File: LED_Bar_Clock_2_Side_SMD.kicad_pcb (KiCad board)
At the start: 2 copper layers, 100 x 100 mm, 51 parts, among them J1 U262-16XN-4BVC11, J2 AVR-ISP-6, SW1 SKHMQKE010, SW2 SW_5_Way, U1 ATtiny84A-SSUR, U2 DS1307Z+, Y1 32.768 kHz

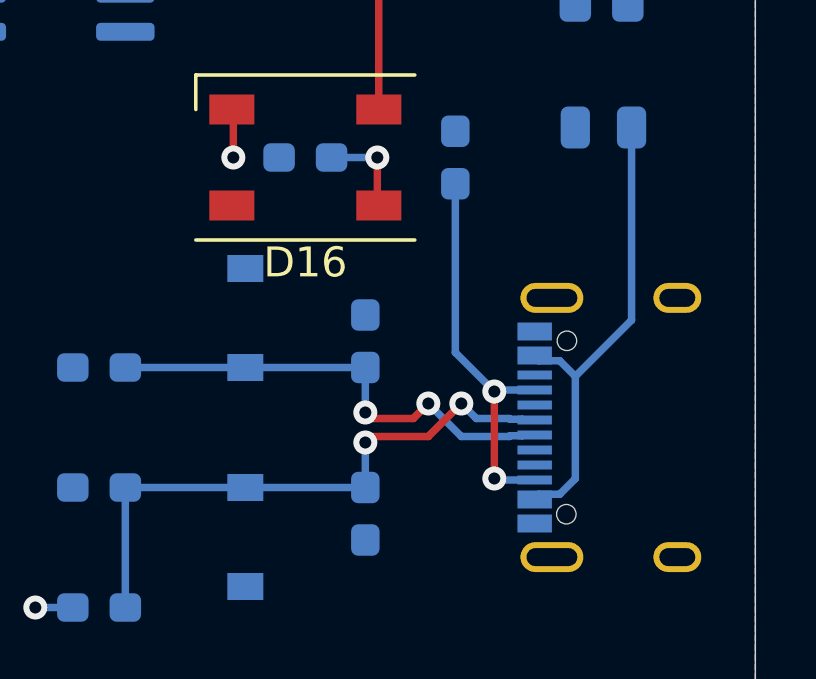
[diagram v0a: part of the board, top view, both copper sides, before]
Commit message: Add B side usb data lines
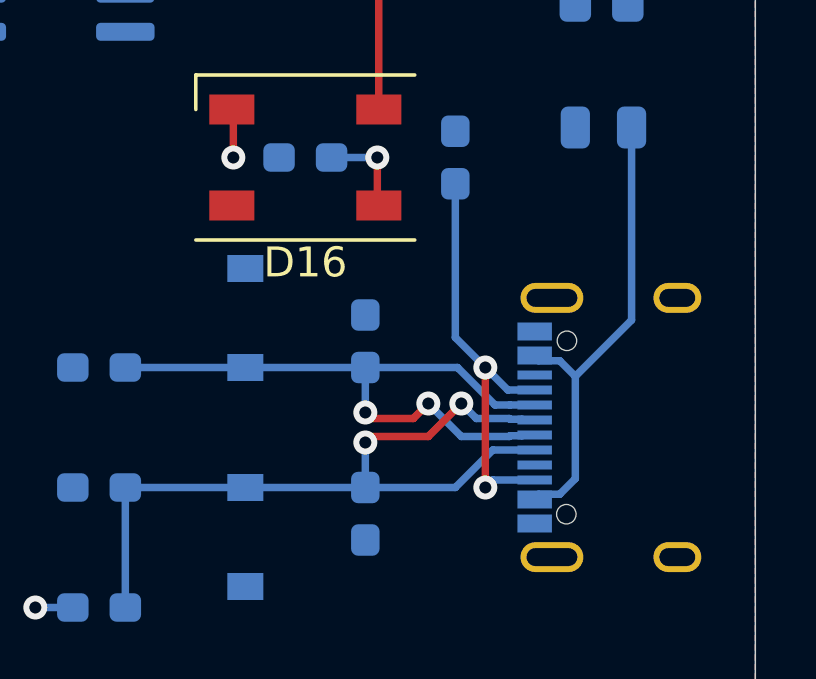
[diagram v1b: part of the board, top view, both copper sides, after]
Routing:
- net Net-(D2-Pad1): track 19.9 -> 26.1 mm
- net Net-(D1-Pad1): track 15.9 -> 22.1 mm
- net Net-(J1-PadA5): track 13.1 -> 14.2 mm
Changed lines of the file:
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@@
     (thickness 1.6)
     (drawings 4)
-    (tracks 205)
+    (tracks 211)
     (zones 0)
     (modules 51)
@@
   (segment (start 61.6 74.45) (end 61.55 74.4) (width 0.25) (layer F.Cu) (net 2))
   (segment (start 61.6 76) (end 61.6 74.45) (width 0.25) (layer F.Cu) (net 2))
-  (via (at 141.3 139.8) (size 0.8) (drill 0.4) (layers F.Cu B.Cu) (net 22))
   (via (at 126 147) (size 0.8) (drill 0.4) (layers F.Cu B.Cu) (net 3))
   (segment (start 137.4 132) (end 135.875 132) (width 0.25) (layer B.Cu) (net 3))
@@
   (segment (start 142.25 141.25) (end 142.225001 141.274999) (width 0.25) (layer B.Cu) (net 4))
   (segment (start 142.645 141.25) (end 142.25 141.25) (width 0.25) (layer B.Cu) (net 4))
+  (segment (start 141.82 140.25) (end 142.645 140.25) (width 0.25) (layer B.Cu) (net 4))
+  (segment (start 141.323002 140.25) (end 141.82 140.25) (width 0.25) (layer B.Cu) (net 4))
+  (segment (start 140.073002 139) (end 141.323002 140.25) (width 0.25) (layer B.Cu) (net 4))
+  (segment (start 137 139) (end 140.073002 139) (width 0.25) (layer B.Cu) (net 4))
   (via (at 140.2 140.2) (size 0.8) (drill 0.4) (layers F.Cu B.Cu) (net 5))
   (segment (start 140.2 140.2) (end 140.7 140.7) (width 0.25) (layer B.Cu) (net 5))
@@
   (segment (start 142.25 140.75) (end 142.225001 140.725001) (width 0.25) (layer B.Cu) (net 5))
   (segment (start 142.645 140.75) (end 142.25 140.75) (width 0.25) (layer B.Cu) (net 5))
+  (segment (start 137 143) (end 140 143) (width 0.25) (layer B.Cu) (net 5))
+  (segment (start 141.25 141.75) (end 142.645 141.75) (width 0.25) (layer B.Cu) (net 5))
+  (segment (start 140 143) (end 141.25 141.75) (width 0.25) (layer B.Cu) (net 5))
   (segment (start 61.55 61.6) (end 61.55 65.55) (width 0.25) (layer F.Cu) (net 7))
   (segment (start 66.45 70.45) (end 66.45 74.4) (width 0.25) (layer F.Cu) (net 7))
@@
   (segment (start 145.875 137.419998) (end 145.875 131) (width 0.25) (layer B.Cu) (net 21))
   (segment (start 144 139.294998) (end 145.875 137.419998) (width 0.25) (layer B.Cu) (net 21))
-  (segment (start 141.3 139.8) (end 141.3 142.7) (width 0.25) (layer F.Cu) (net 22))
-  (segment (start 141.3 142.7) (end 141.3 142.7) (width 0.25) (layer F.Cu) (net 22))
-  (via (at 141.3 142.7) (size 0.8) (drill 0.4) (layers F.Cu B.Cu) (net 22))
-  (segment (start 141.35 139.75) (end 141.3 139.8) (width 0.25) (layer B.Cu) (net 22))
-  (segment (start 142.645 139.75) (end 141.35 139.75) (width 0.25) (layer B.Cu) (net 22))
-  (segment (start 141.35 142.75) (end 141.3 142.7) (width 0.25) (layer B.Cu) (net 22))
-  (segment (start 142.645 142.75) (end 141.35 142.75) (width 0.25) (layer B.Cu) (net 22))
-  (segment (start 140 138.5) (end 141.3 139.8) (width 0.25) (layer B.Cu) (net 22))
-  (segment (start 140 132.875) (end 140 138.5) (width 0.25) (layer B.Cu) (net 22))
+  (via (at 141 139) (size 0.8) (drill 0.4) (layers F.Cu B.Cu) (net 22))
+  (via (at 141 143) (size 0.8) (drill 0.4) (layers F.Cu B.Cu) (net 22))
+  (segment (start 141.25 142.75) (end 141 143) (width 0.25) (layer B.Cu) (net 22))
+  (segment (start 142.645 142.75) (end 141.25 142.75) (width 0.25) (layer B.Cu) (net 22))
+  (segment (start 141.75 139.75) (end 141 139) (width 0.25) (layer B.Cu) (net 22))
+  (segment (start 142.645 139.75) (end 141.75 139.75) (width 0.25) (layer B.Cu) (net 22))
+  (segment (start 141 143) (end 141 139) (width 0.25) (layer F.Cu) (net 22))
+  (segment (start 140 138) (end 141 139) (width 0.25) (layer B.Cu) (net 22))
+  (segment (start 140 132.875) (end 140 138) (width 0.25) (layer B.Cu) (net 22))
   (zone (net 3) (net_name +5V) (layer F.Cu) (hatch edge 0.508)
     (connect_pads (clearance 0.5))
     (min_thickness 0.25)
-    (fill yes (arc_segments 32) (thermal_gap 0.5) (thermal_bridge_width 0.5) (smoothing fillet) (radius 5))
+    (fill (arc_segments 32) (thermal_gap 0.5) (thermal_bridge_width 0.5) (smoothing fillet) (radius 5))
     (polygon
       (pts
@@
     (connect_pads (clearance 0.5))
     (min_thickness 0.25)
-    (fill yes (arc_segments 32) (thermal_gap 0.5) (thermal_bridge_width 0.5) (smoothing fillet) (radius 5))
+    (fill (arc_segments 32) (thermal_gap 0.5) (thermal_bridge_width 0.5) (smoothing fillet) (radius 5))
     (polygon
       (pts

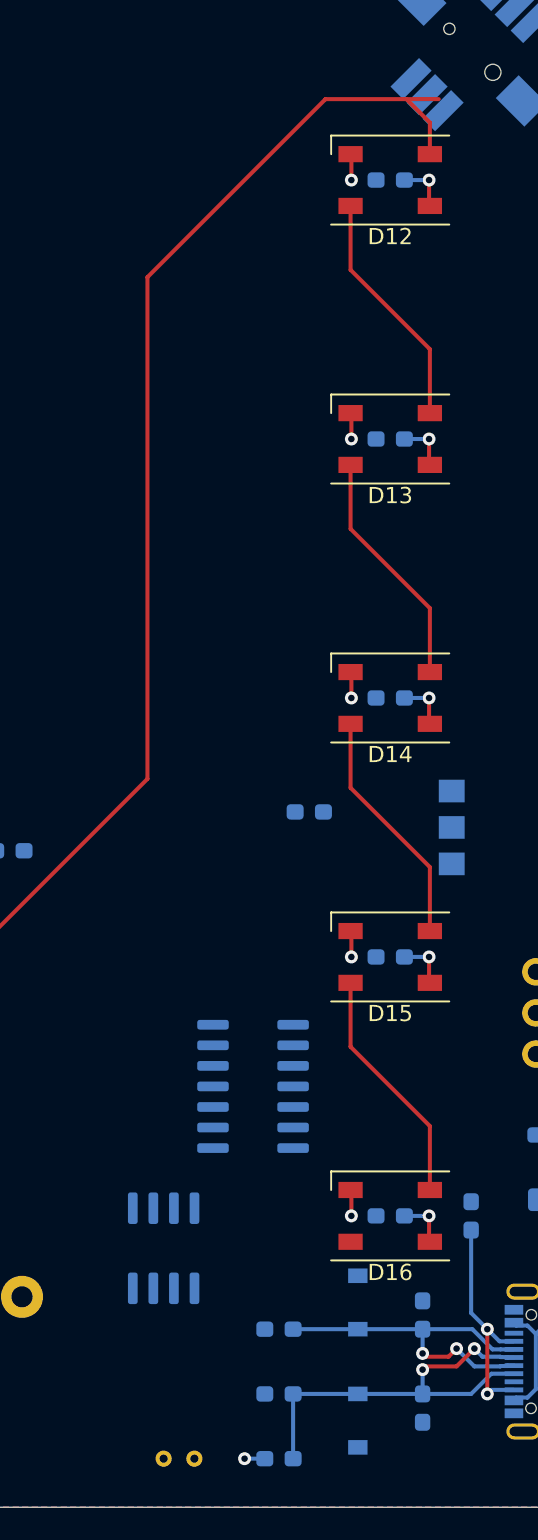
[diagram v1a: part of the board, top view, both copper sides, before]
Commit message: Flip crystal footprint
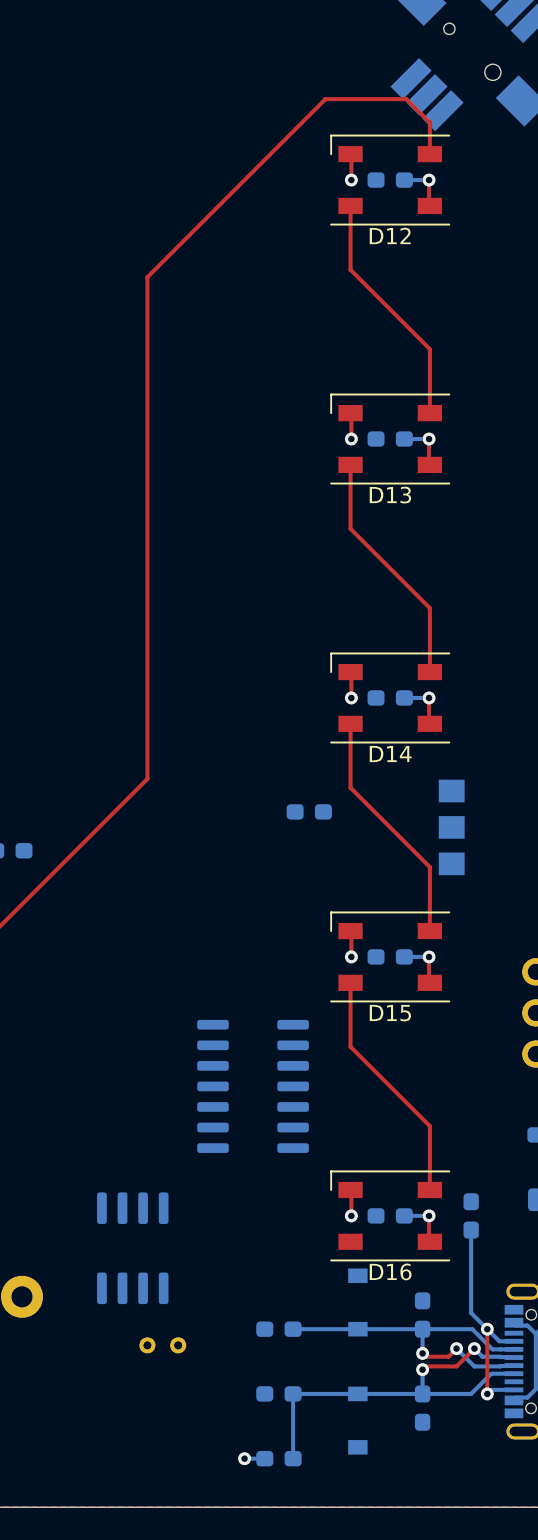
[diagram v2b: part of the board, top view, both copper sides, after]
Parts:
- moved Y1 7.06 mm to (121.9, 140.0), turned to 180 degrees
- moved U2 1.91 mm to (119.1, 134.0)
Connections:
- Y1 pad 1: Net-(U2-Pad2) -> Net-(U2-Pad1)
- Y1 pad 2: Net-(U2-Pad1) -> Net-(U2-Pad2)
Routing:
- net Net-(D11-Pad2): track 89.2 -> 87.2 mm
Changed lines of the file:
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@@
     (mod_text_size 1 1)
     (mod_text_width 0.15)
-    (pad_size 1.524 1.524)
-    (pad_drill 0.762)
+    (pad_size 1 1)
+    (pad_drill 0.5)
     (pad_to_mask_clearance 0.051)
     (solder_mask_min_width 0.25)
@@
   )
   (module Package_SO:SOIC-8_3.9x4.9mm_P1.27mm (layer B.Cu)
-    (at 121 134 90)
+    (at 119.095 134 90)
     (descr "SOIC, 8 Pin (JEDEC MS-012AA, https://www.analog.com/media/en/package-pcb-resources/package/pkg_pdf/soic_narrow-r/r_8.pdf), generated with kicad-footprint-generator ipc_gullwing_generator.py")
     (tags "SOIC SO")
@@
   )
   (module Crystal:Crystal_DS26_D2.0mm_L6.0mm_Horizontal (layer B.Cu)
-    (at 121 147)
+    (at 121.9 140 180)
     (descr "Crystal THT DS26 6.0mm length 2.0mm diameter http://www.microcrystal.com/images/_Product-Documentation/03_TF_metal_Packages/01_Datasheet/DS-Series.pdf")
     (tags ['DS26'])
@@
     (fp_line (start 2.7 -8.8) (end 2.7 0.8) (layer B.CrtYd) (width 0.05))
     (fp_line (start 2.7 0.8) (end -0.8 0.8) (layer B.CrtYd) (width 0.05))
-    (pad 1 thru_hole circle (at 0 0) (size 1 1) (drill 0.5) (layers *.Cu *.Mask)
+    (pad 1 thru_hole circle (at 0 0 180) (size 1 1) (drill 0.5) (layers *.Cu *.Mask)
+      (net 36 "Net-(U2-Pad1)"))
+    (pad 2 thru_hole circle (at 1.9 0 180) (size 1 1) (drill 0.5) (layers *.Cu *.Mask)
       (net 37 "Net-(U2-Pad2)"))
-    (pad 2 thru_hole circle (at 1.9 0) (size 1 1) (drill 0.5) (layers *.Cu *.Mask)
-      (net 36 "Net-(U2-Pad1)"))
     (model ${KISYS3DMOD}/Crystal.3dshapes/Crystal_DS26_D2.0mm_L6.0mm_Horizontal.wrl
       (at (xyz 0 0 0))
@@
   (segment (start 99 121) (end 104 121) (width 0.25) (layer F.Cu) (net 15))
   (segment (start 104 121) (end 120 105) (width 0.25) (layer F.Cu) (net 15))
-  (segment (start 131 63) (end 138 63) (width 0.25) (layer F.Cu) (net 15))
   (segment (start 131 63) (end 120 74) (width 0.25) (layer F.Cu) (net 15))
   (segment (start 120 74) (end 120 105) (width 0.25) (layer F.Cu) (net 15))
+  (segment (start 136 63) (end 131 63) (width 0.25) (layer F.Cu) (net 15))
   (segment (start 132.55 73.55) (end 137.45 78.45) (width 0.25) (layer F.Cu) (net 16))
   (segment (start 137.45 78.45) (end 137.45 82.4) (width 0.25) (layer F.Cu) (net 16))
@@
     (connect_pads (clearance 0.5))
     (min_thickness 0.25)
-    (fill (arc_segments 32) (thermal_gap 0.5) (thermal_bridge_width 0.5) (smoothing fillet) (radius 5))
+    (fill yes (arc_segments 32) (thermal_gap 0.5) (thermal_bridge_width 0.5) (smoothing fillet) (radius 5))
     (polygon
       (pts
@@
     (connect_pads (clearance 0.5))
     (min_thickness 0.25)
-    (fill (arc_segments 32) (thermal_gap 0.5) (thermal_bridge_width 0.5) (smoothing fillet) (radius 5))
+    (fill yes (arc_segments 32) (thermal_gap 0.5) (thermal_bridge_width 0.5) (smoothing fillet) (radius 5))
     (polygon
       (pts

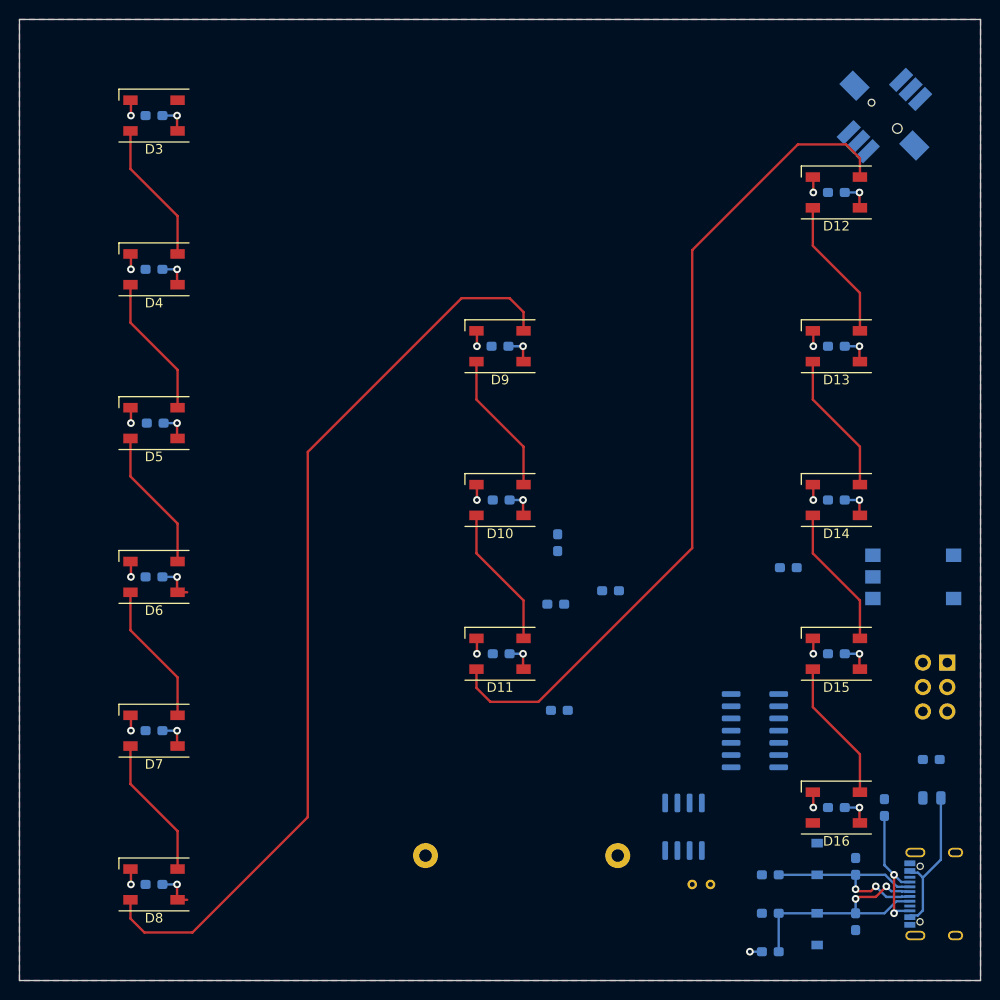
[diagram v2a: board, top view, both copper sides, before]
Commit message: an attempt at better placement for right edge
(icsp header, switches, power circuitry)
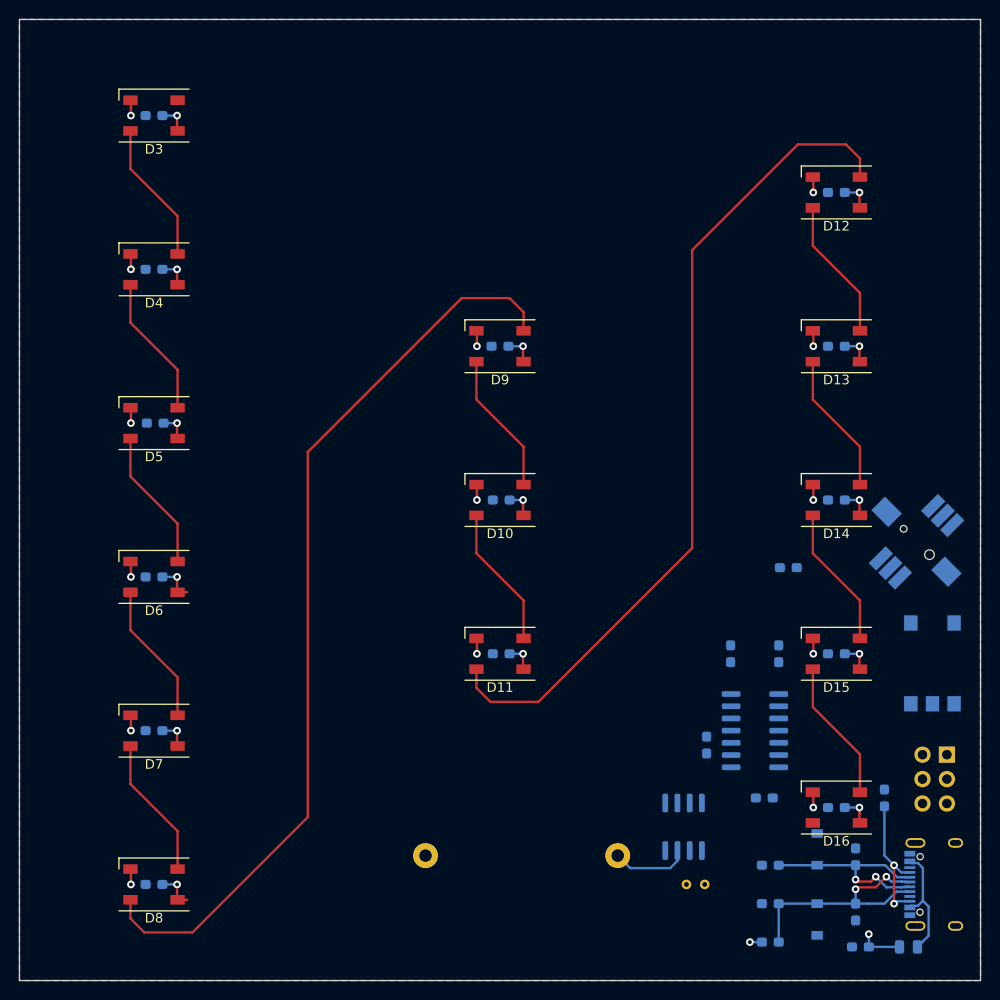
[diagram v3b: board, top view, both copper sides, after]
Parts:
- moved SW2 44.5 mm to (143.3, 104.3)
- moved C1 26.8 mm to (127.5, 131.0)
- moved R6 26.1 mm to (121.5, 125.5)
- moved R5 23.6 mm to (129.0, 116.0), turned to 270 degrees
- moved C3 20.8 mm to (137.5, 146.5), turned to 180 degrees
- moved R4 18.9 mm to (124.0, 116.0), turned to 270 degrees
- moved F1 15.7 mm to (142.5, 146.5)
- moved J2 9.58 mm to (146.5, 126.5)
- moved SW1 9.22 mm to (145.0, 117.0), turned to 270 degrees
- moved D1 1.00 mm to (133.0, 136.3)
- moved D2 1.00 mm to (133.0, 143.7)
- moved J1 1.00 mm to (150.0, 140.0)
- moved R1 1.00 mm to (128.1, 146.0)
- moved R2 1.00 mm to (128.1, 142.0)
- moved R3 1.00 mm to (128.1, 138.0)
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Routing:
- net Net-(BT1-Pad1): track 0.00 -> 8.13 mm
- net +5V: track 47.3 -> 51.8 mm, vias 15 -> 16
- net Net-(F1-Pad2): track 15.8 -> 12.3 mm

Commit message: Finish pcb routing
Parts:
- removed C2: 104, Capacitor_SMD:C_0603_1608Metric_Pad1.05x0.95mm_HandSolder
- added REF**: MountingHole_3.2mm_M3_Pad_Via, MountingHole:MountingHole_3.2mm_M3_Pad_Via, F.Cu at (55.0, 116.0)
- added REF**: MountingHole_3.2mm_M3_Pad_Via, MountingHole:MountingHole_3.2mm_M3_Pad_Via, F.Cu at (145.0, 116.0)
- moved SW2 54.3 mm to (100.6, 70.9), turned to 315 degrees
- moved R6 40.3 mm to (143.9, 92.0), turned to 180 degrees
- moved R5 19.9 mm to (113.1, 128.0), turned to 0 degrees
- moved SW1 17.0 mm to (145.2, 100.0)
- moved R4 13.5 mm to (117.9, 128.0), turned to 180 degrees
- moved U1 4.76 mm to (122.0, 122.5), turned to 90 degrees
- moved C1 2.72 mm to (125.8, 128.9), turned to 270 degrees
- moved J2 2.55 mm to (147.0, 124.0)
- moved BT1 2.25 mm to (97.8, 137.0)
- moved F1 1.64 mm to (144.1, 147.0)
- moved R7 1.12 mm to (140.0, 132.1)
- moved C3 0.80 mm to (138.1, 147.0)
- moved Y1 0.78 mm to (120.8, 139.4)
- moved U2 0.50 mm to (118.6, 134.0)
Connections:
- net Net-(R2-Pad2) renamed /D+
- net Net-(R3-Pad2) renamed /D-
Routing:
- net Net-(SW2-Pad6): track 0.00 -> 120.7 mm
- net Net-(J2-Pad5): track 0.00 -> 69.1 mm
- net Net-(SW2-Pad4): track 0.00 -> 61.9 mm
- net Net-(J2-Pad3): track 0.00 -> 59.3 mm
- net Net-(SW2-Pad1): track 0.00 -> 55.8 mm
- net Net-(SW2-Pad2): track 0.00 -> 54.7 mm
- net Net-(SW2-Pad3): track 0.00 -> 53.6 mm
- net Net-(J2-Pad4): track 0.00 -> 36.8 mm
- net Net-(J2-Pad1): track 0.00 -> 31.1 mm
- net Net-(D16-Pad2): track 0.00 -> 25.7 mm, vias 0 -> 1
- net /D+: track 0.00 -> 18.9 mm, vias 0 -> 2
- net /D-: track 0.00 -> 18.9 mm, vias 0 -> 2
- net Net-(D8-Pad2): track 95.6 -> 113.8 mm, vias 0 -> 4
- net Net-(D11-Pad2): track 87.2 -> 104.8 mm, vias 0 -> 4
- net +5V: track 51.8 -> 60.9 mm, vias 16 -> 21
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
